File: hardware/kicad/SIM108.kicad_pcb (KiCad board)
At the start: 2 copper layers, 100 x 85 mm, 114 parts, among them J1 Screw_Terminal_01x09, J2 CAN, Q1 BC547, Q10 BC337-40, Q11 BC547, Q12 BC337-40, Q13 BC547, Q14 BC337-40, Q15 BC547, Q16 BC337-40, Q2 BC337-40, Q3 BC547, Q4 BC337-40, Q5 BC547, Q6 BC337-40, Q7 BC547, Q8 BC337-40, Q9 BC547, SW1 PRG, SW2 INSTANCE, SW3 BUS, U1 MCP2551-I-P, U10 SFH617A-1, U11 MAX6816, U12 SFH617A-1, U13 MAX6816, U14 SFH617A-1, U15 MAX6816, U16 SFH617A-1, U17 MAX6816, U18 SFH617A-1, U19 MAX6816, U2 TMR_2411, U20 SFH617A-1, U21 MAX6816, U3 MAX6816, U4 74HC595, U5 Teensy_3.2, U6 SFH617A-1, U7 MAX6816, U8 SFH617A-1, U9 MAX6816

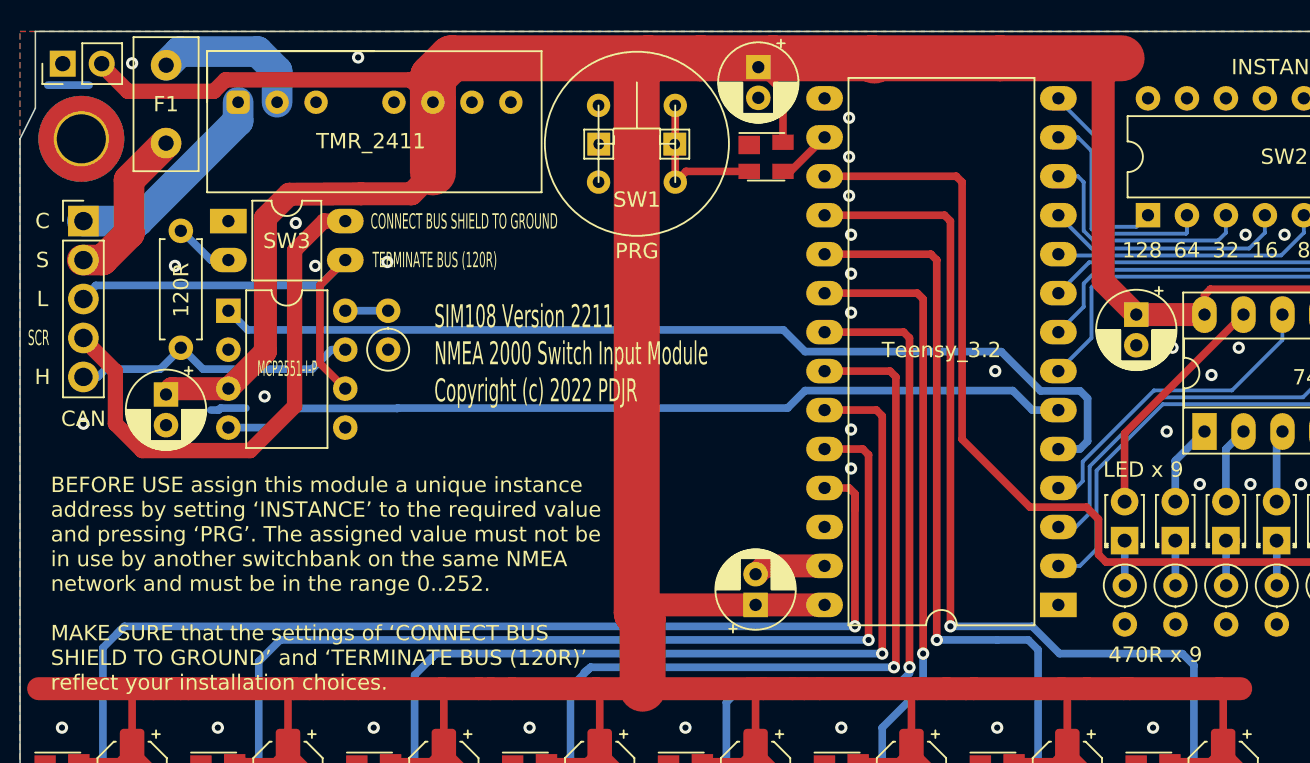
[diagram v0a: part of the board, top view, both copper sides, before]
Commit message: Add jumper alternative to SW2
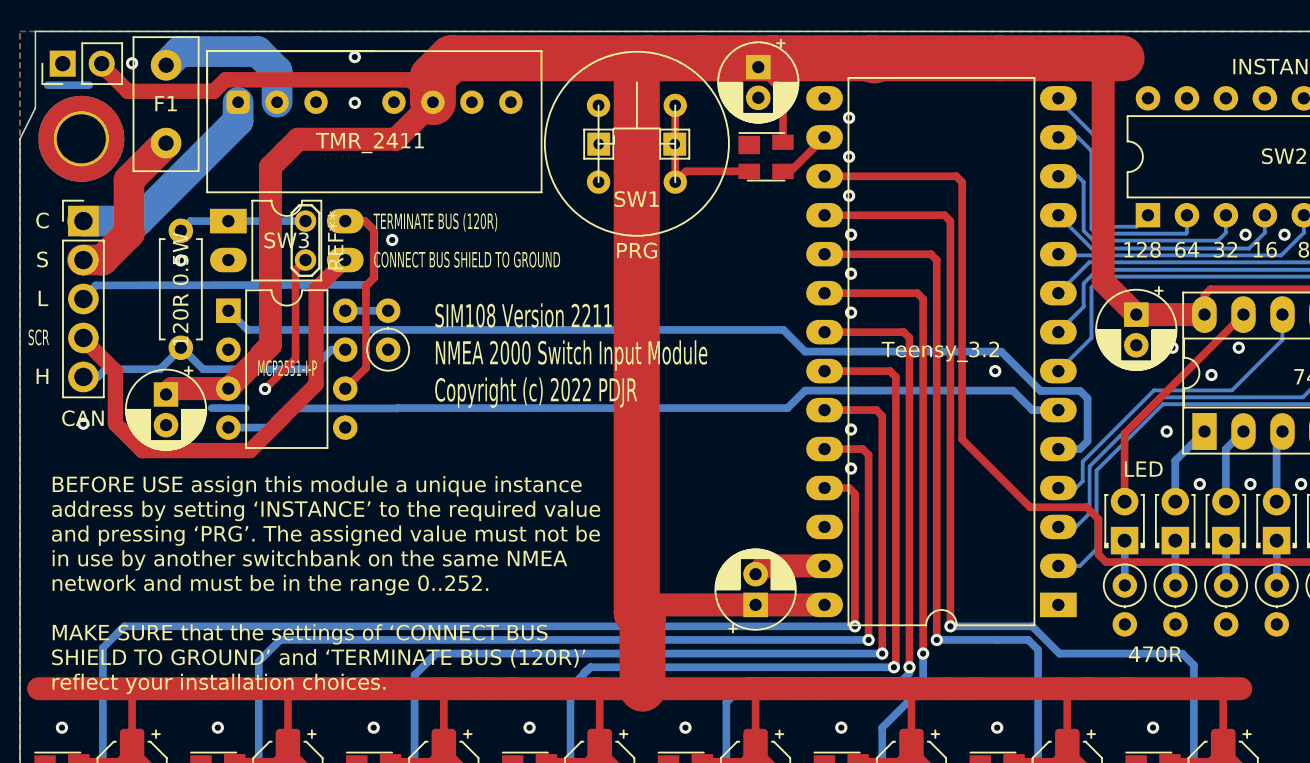
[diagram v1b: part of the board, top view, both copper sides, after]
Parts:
- added REF**: TestPoint_2Pads_Pitch2.54mm_Drill0.8mm, TestPoint:TestPoint_2Pads_Pitch2.54mm_Drill0.8mm, F.Cu at (38.6, 32.4)
- D1: value LED x 9 -> LED
- R2: renamed from Re; value 120R -> 120R 0.5W
- R28: value 470R x 9 -> 470R
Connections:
- SW3 pad 1: GND -> /TERM_A
- SW3 pad 2: /TERM_A -> GND
- SW3 pad 3: /CAN_L -> /CAN_SCR
- SW3 pad 4: /CAN_SCR -> /CAN_L
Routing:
- net /CAN_L: track 27.9 -> 38.3 mm
- net GND: track 9.82 -> 19.5 mm
- net /TERM_A: track 3.84 -> 8.39 mm
- net /CAN_SCR: track 34.3 -> 31.5 mm
- net +5V: track 424.3 -> 421.7 mm

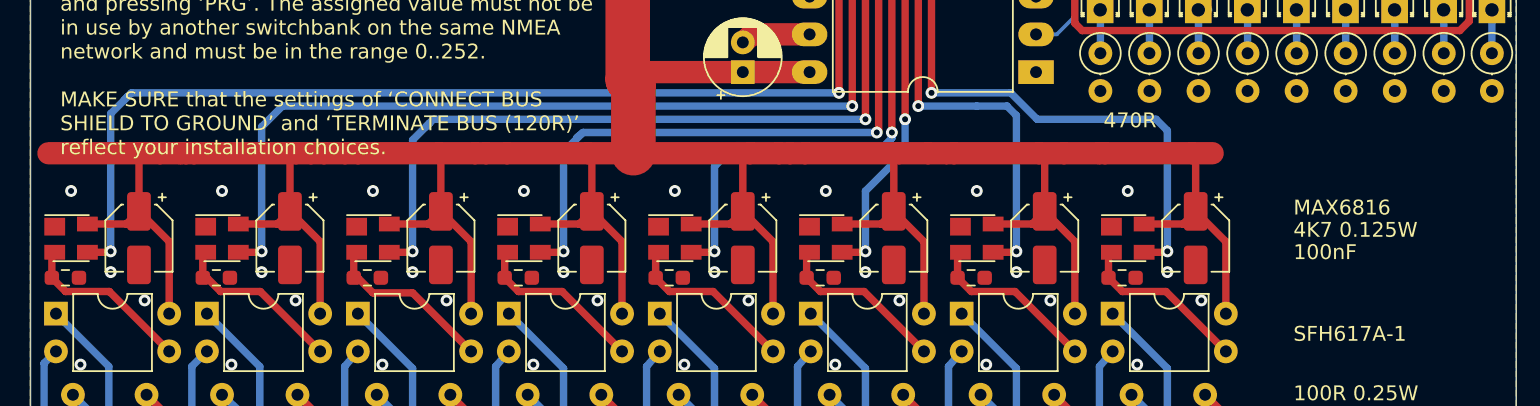
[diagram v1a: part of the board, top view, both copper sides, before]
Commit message: Swap passive SMD for TH
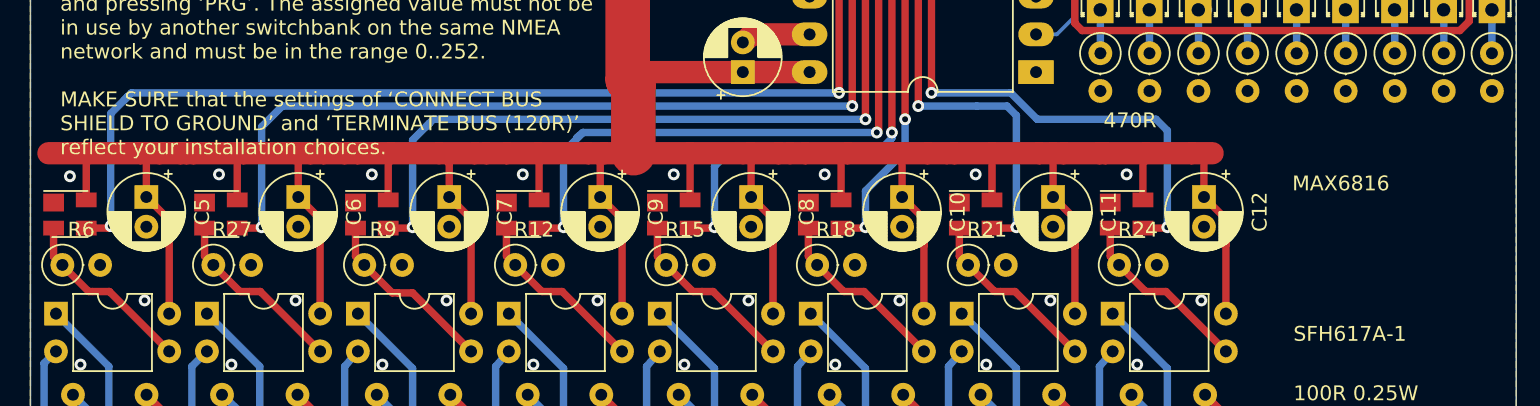
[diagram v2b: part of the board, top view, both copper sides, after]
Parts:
- C10, C11, C12, C5, C6, C7, C8, C9: footprint Capacitor_SMD:CP_Elec_4x4.5 -> Capacitor_THT:CP_Radial_D5.0mm_P2.00mm
- R12, R15, R18, R21, R24, R27, R6, R9: footprint Resistor_SMD:R_0603_1608Metric_Pad0.98x0.95mm_HandSolder -> Resistor_THT:R_Axial_DIN0207_L6.3mm_D2.5mm_P2.54mm_Vertical
- moved C8 2.82 mm to (68.5, 65.8)
- moved C9 2.82 mm to (58.3, 65.8)
- moved C10 2.82 mm to (78.7, 65.8)
- moved C11 2.82 mm to (88.8, 65.8)
- moved C12 2.82 mm to (99.0, 65.8)
- moved C6 2.82 mm to (38.0, 65.8)
- moved C7 2.82 mm to (48.2, 65.8)
- moved C5 2.81 mm to (27.8, 65.8)
- moved U15 1.63 mm to (73.5, 66.9)
- moved U11 1.63 mm to (53.1, 66.9)
- moved U13 1.63 mm to (63.3, 66.9)
- moved U21 1.63 mm to (32.8, 66.9)
- moved U7 1.63 mm to (22.7, 66.9)
- moved U9 1.63 mm to (43.0, 66.9)
- moved U17 1.63 mm to (83.6, 66.9)
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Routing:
- net +5V: track 421.7 -> 419.3 mm
- net /CH0: track 72.6 -> 71.0 mm
- net /CH4: track 48.0 -> 46.4 mm
- net /CH5: track 41.3 -> 39.7 mm
- net /CH3: track 55.3 -> 53.8 mm
- net /CH2: track 59.9 -> 58.4 mm
- net /CH1: track 65.4 -> 63.8 mm
- net /CH7: track 61.4 -> 59.9 mm
- net /CH6: track 49.8 -> 48.3 mm
- net Net-(R6-Pad1): track 11.7 -> 12.3 mm
- net Net-(R21-Pad1): track 11.7 -> 12.3 mm
- net Net-(R18-Pad1): track 11.7 -> 12.3 mm
- net Net-(R9-Pad1): track 11.7 -> 12.3 mm
- net Net-(R15-Pad1): track 11.7 -> 12.3 mm
- net Net-(R12-Pad1): track 11.7 -> 12.3 mm
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
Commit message: PCB silk update
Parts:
- added ?: , , F.Cu at (107.9, 64.8)
- added ?: , , F.Cu at (109.1, 69.0)
- U5: value Teensy_3.2 -> Teensy 4.0
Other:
- board text added: "SIM108 Version 2212 NMEA 2000 Switch Input Module Copyright (c) 2022 PDJR"
- board text removed: "SIM108 Version 2211 NMEA 2000 Switch Input Module Copyright (c) 2022 PDJR"

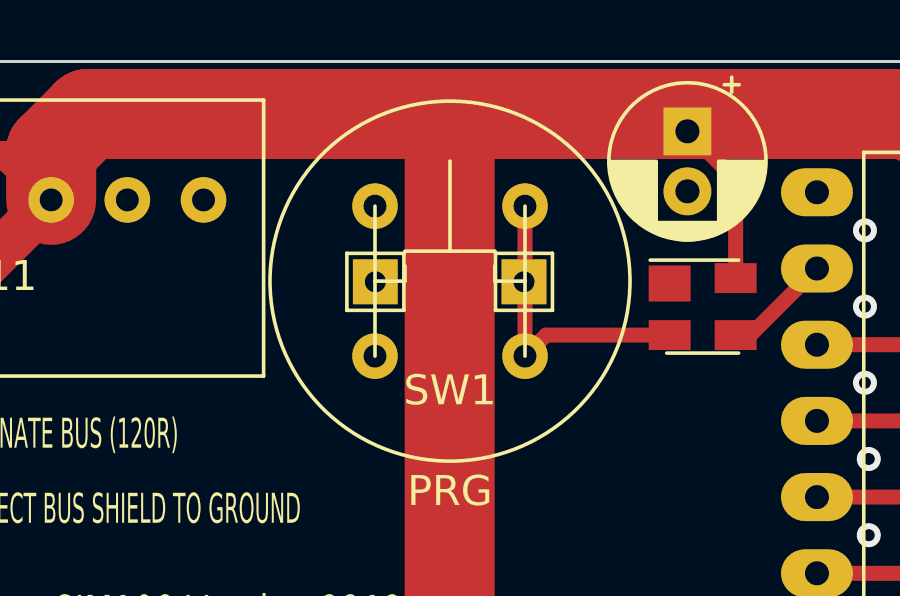
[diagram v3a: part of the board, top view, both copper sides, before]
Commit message: Revise for 3.3V
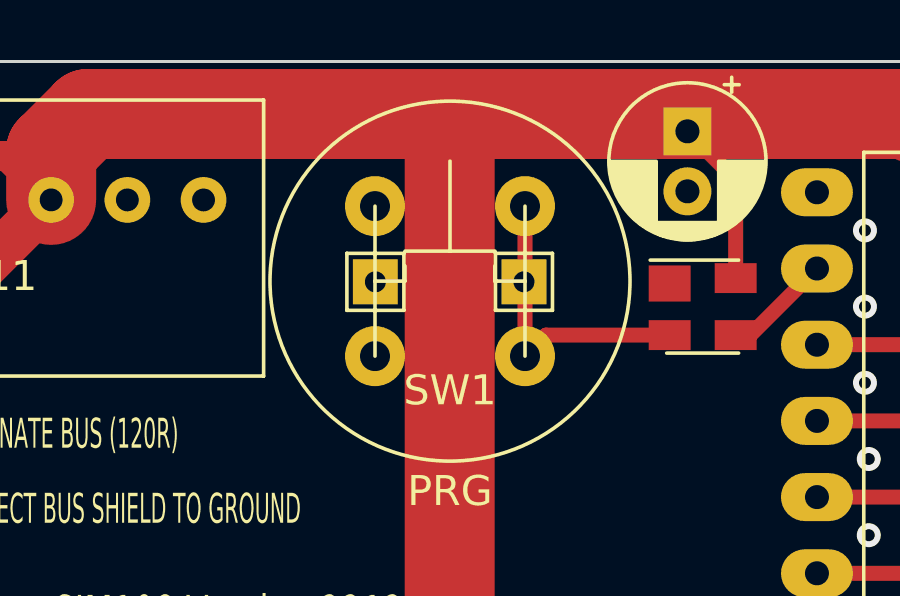
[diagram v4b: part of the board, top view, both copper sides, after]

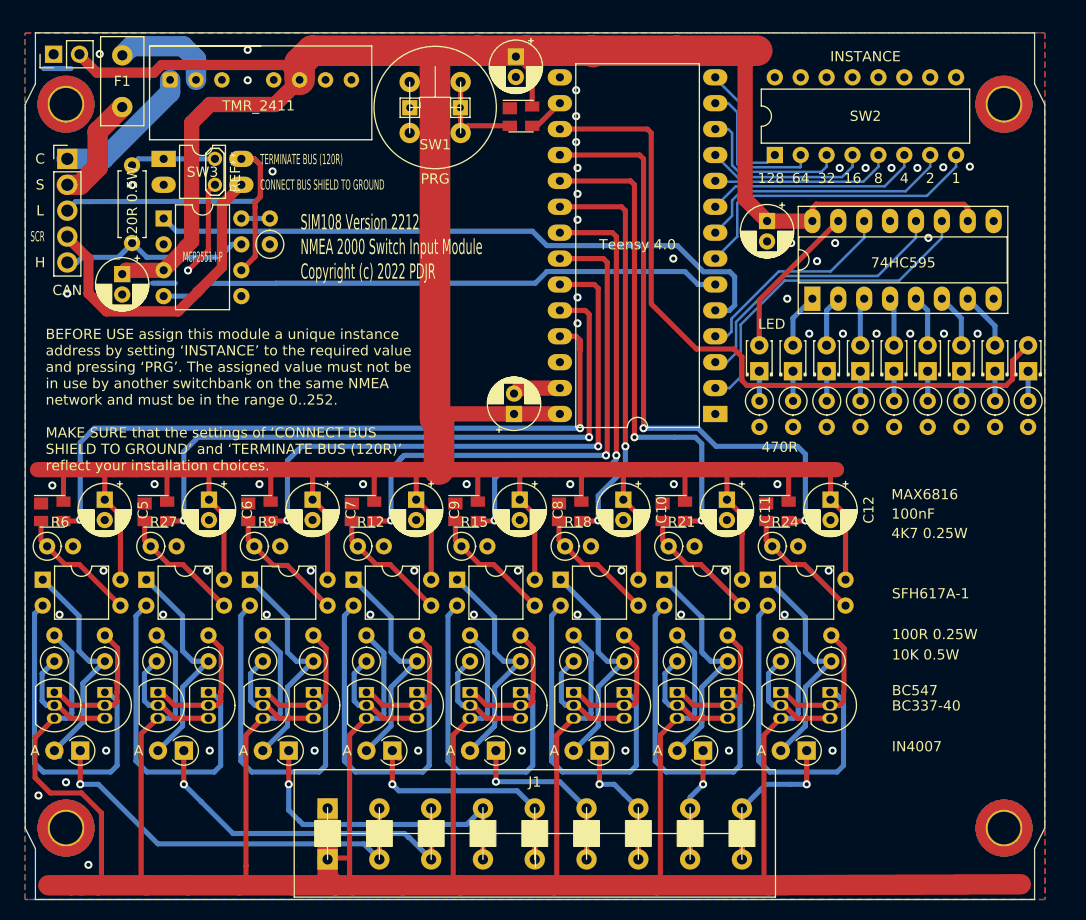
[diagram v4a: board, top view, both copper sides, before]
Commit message: Migrate to Teens 4.0
3.3V inputs
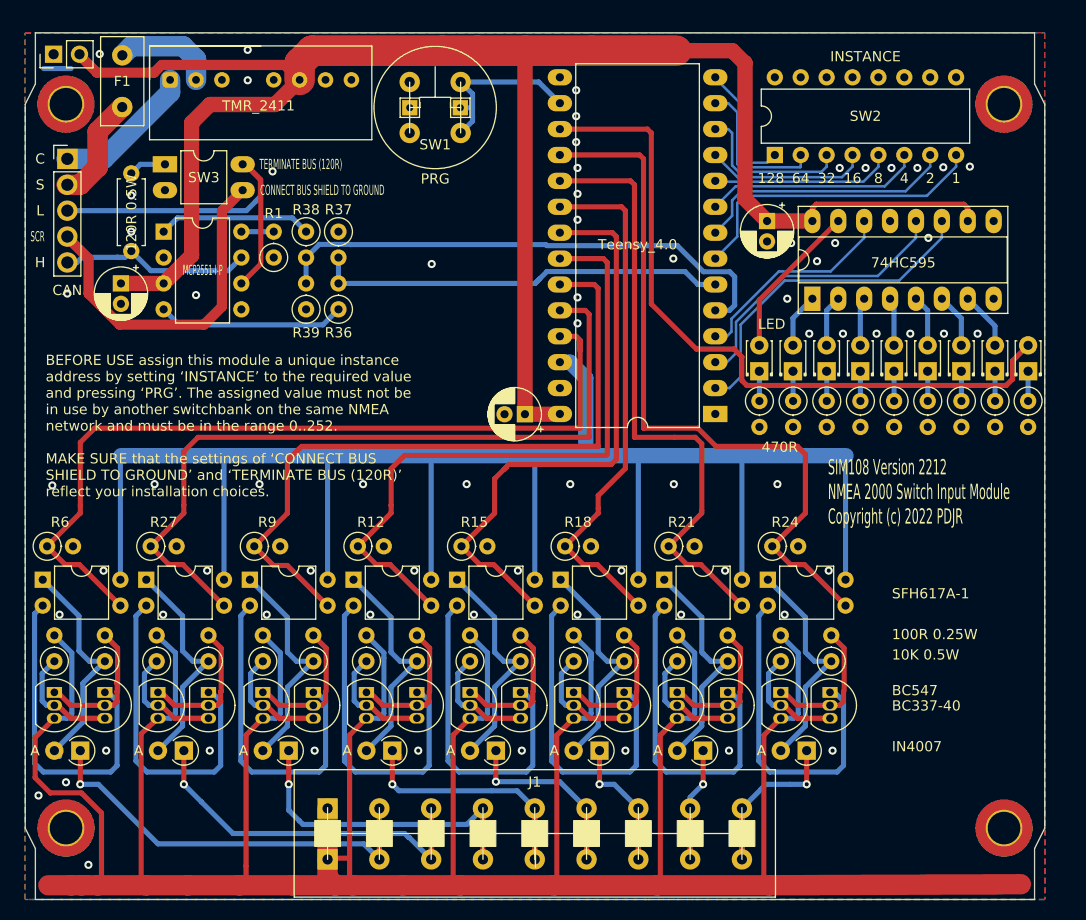
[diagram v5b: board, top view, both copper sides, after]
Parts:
- removed ? (x2): , 
- removed C10, C11, C12, C2, C5, C6, C7, C8, C9: 100nF, Capacitor_THT:CP_Radial_D5.0mm_P2.00mm
- removed the REF** at (38.6, 32.4)
- removed U11, U13, U15, U17, U19, U21, U3, U7, U9: MAX6816, Package_TO_SOT_SMD:SOT-143
- added R36: 2K2 0.125W, Resistor_THT:R_Axial_DIN0207_L6.3mm_D2.5mm_P2.54mm_Vertical, F.Cu at (50.7, 47.1)
- added R37: 3K3 0.125W, Resistor_THT:R_Axial_DIN0207_L6.3mm_D2.5mm_P2.54mm_Vertical, F.Cu at (50.7, 39.5)
- added R38: 2K2 0.125W, Resistor_THT:R_Axial_DIN0207_L6.3mm_D2.5mm_P2.54mm_Vertical, F.Cu at (47.5, 39.5)
- added R39: 3K3 0.125W, Resistor_THT:R_Axial_DIN0207_L6.3mm_D2.5mm_P2.54mm_Vertical, F.Cu at (47.5, 47.1)
- U5: value Teensy 4.0 -> Teensy_4.0
- moved R1 1.35 mm to (44.4, 42.0)
- moved U1 1.30 mm to (33.6, 39.5)
- moved C3 1.07 mm to (69.0, 57.4), turned to 180 degrees
- moved C1 0.92 mm to (29.4, 44.6)
- moved R2 0.79 mm to (30.4, 41.4)
- moved SW3 0.55 mm to (33.7, 32.9)
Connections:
- R12 pad 1: Net-(R12-Pad1) -> /CH3
- R15 pad 1: Net-(R15-Pad1) -> /CH4
- R18 pad 1: Net-(R18-Pad1) -> /CH5
- R21 pad 1: Net-(R21-Pad1) -> /CH6
- R24 pad 1: Net-(R24-Pad1) -> /CH7
- R27 pad 1: Net-(R27-Pad1) -> /CH1
- R6 pad 1: Net-(R6-Pad1) -> /CH0
- R9 pad 1: Net-(R9-Pad1) -> /CH2
- REF** pad 1: Net-(SW1-Pad2) -> /PRG
- SW1 pad 2: Net-(SW1-Pad2) -> /PRG
- U1 pad 1: /CAN_TX -> Net-(R38-Pad1)
- U1 pad 4: /CAN_RX -> Net-(R36-Pad1)
- U10 pad 3: Net-(R12-Pad1) -> /CH3
- U10 pad 4: +5V -> /3V3
- U12 pad 3: Net-(R15-Pad1) -> /CH4
- U12 pad 4: +5V -> /3V3
- U14 pad 3: Net-(R18-Pad1) -> /CH5
- U14 pad 4: +5V -> /3V3
- U16 pad 3: Net-(R21-Pad1) -> /CH6
- U16 pad 4: +5V -> /3V3
- U18 pad 3: Net-(R24-Pad1) -> /CH7
- U18 pad 4: +5V -> /3V3
- U20 pad 3: Net-(R27-Pad1) -> /CH1
- U20 pad 4: +5V -> /3V3
- U5 pad 26: Net-(U5-Pad26) -> /3V3
- U6 pad 3: Net-(R6-Pad1) -> /CH0
- U6 pad 4: +5V -> /3V3
- U8 pad 3: Net-(R9-Pad1) -> /CH2
- U8 pad 4: +5V -> /3V3
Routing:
- net +5V: track 419.3 -> 184.3 mm
- net /3V3: track 0.00 -> 182.4 mm
- net Net-(R36-Pad1): track 0.00 -> 18.4 mm
- net GND: track 19.5 -> 2.76 mm, vias 69 -> 70
- net Net-(R38-Pad1): track 0.00 -> 15.1 mm
- net /CAN_RX: track 55.6 -> 41.1 mm
- net /PRG: track 3.63 -> 17.8 mm
- net Net-(R6-Pad1): track 12.3 -> 0.00 mm
- net Net-(R27-Pad1): track 12.3 -> 0.00 mm
- net Net-(R21-Pad1): track 12.3 -> 0.00 mm
- net Net-(R18-Pad1): track 12.3 -> 0.00 mm
- net Net-(R15-Pad1): track 12.3 -> 0.00 mm
- net Net-(R12-Pad1): track 12.3 -> 0.00 mm
- net Net-(R9-Pad1): track 12.3 -> 0.00 mm
- net Net-(R24-Pad1): track 12.3 -> 0.00 mm
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
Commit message: Tweaks
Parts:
- removed the REF** at (57.7, 27.3)
- removed the REF** at (62.7, 27.3)
- SW1: footprint PDJR_Switches:PCB_PUSH_BUTTON_10mm -> Button_Switch_THT:SW_TH_Tactile_Omron_B3F-10xx
- moved SW1 10.9 mm to (67.1, 24.4), turned to 270 degrees
- moved R2 0.89 mm to (30.4, 40.5)
- moved J2 0.54 mm to (24.1, 32.9)
- moved U2 0.23 mm to (34.2, 24.4)
- moved C1 0.13 mm to (29.4, 44.7)
- moved R1 0.13 mm to (44.4, 42.2)
- moved R36 0.13 mm to (50.7, 47.2)
- moved R37 0.13 mm to (50.7, 39.6)
- moved R38 0.13 mm to (47.5, 39.6)
- moved R39 0.13 mm to (47.5, 47.2)
- moved SW3 0.13 mm to (33.6, 32.9)
- moved U1 0.13 mm to (33.6, 39.6)
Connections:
- SW1 pad 1: GND -> /PRG
- SW1 pad 2: /PRG -> Net-(SW1-Pad2)
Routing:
- net /PRG: track 17.8 -> 6.35 mm
- net /CAN_L: track 37.7 -> 39.7 mm
- net +5V: track 184.3 -> 185.6 mm
- net Net-(R36-Pad1): track 18.4 -> 19.7 mm
- net /CAN_TX: track 51.3 -> 52.5 mm
- net Net-(F1-Pad1): track 10.7 -> 11.4 mm
- net /CAN_RX: track 41.1 -> 40.5 mm
- net GND: vias 70 -> 66
